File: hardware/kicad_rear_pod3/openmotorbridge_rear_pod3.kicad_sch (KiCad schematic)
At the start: 9 parts, among them J1 POGO_6PIN_MATRIX, J3 MM8030_2G4, J4 MM8030_LORA, J5 MM8030_GNSS, U1 ESP32-C3-WROOM-02U, U2 MAX-M10S, U3 SX1262, U4 DS2401

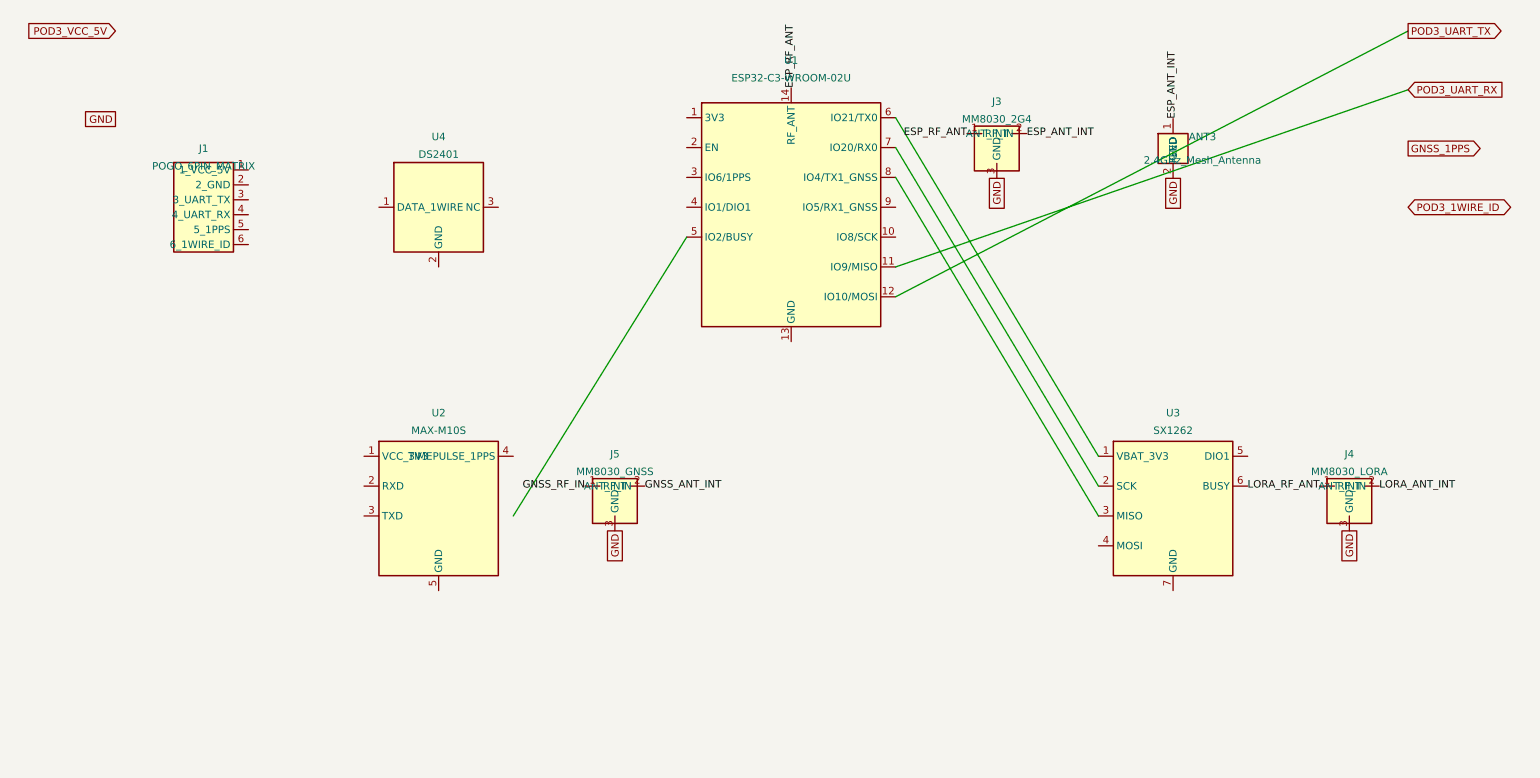
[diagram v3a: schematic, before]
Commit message: feat(pcb): resize OMM transceiver board to 55x48mm and pre-place components
- Resized Edge.Cuts to 55.0 x 48.0 mm (R = 2.5 mm)
- Removed obsolete chip antennas (ANT1, ANT2, ANT3) and mechanical switch (J3)
- Replaced J4 (LoRa) and J5 (GNSS) with U.FL footprints
- Replaced U1 with ESP32-C3-WROOM-02U footprint
- Positioned 4x M2 mounting holes matching sled standoffs: H1/H2 at X=103mm, H3/H4 at X=149mm
- Pre-placed components into clean functional zones (Interface, GNSS, LoRa, ESP32)
- Re-rendered photorealistic top and bottom 3D raytraces
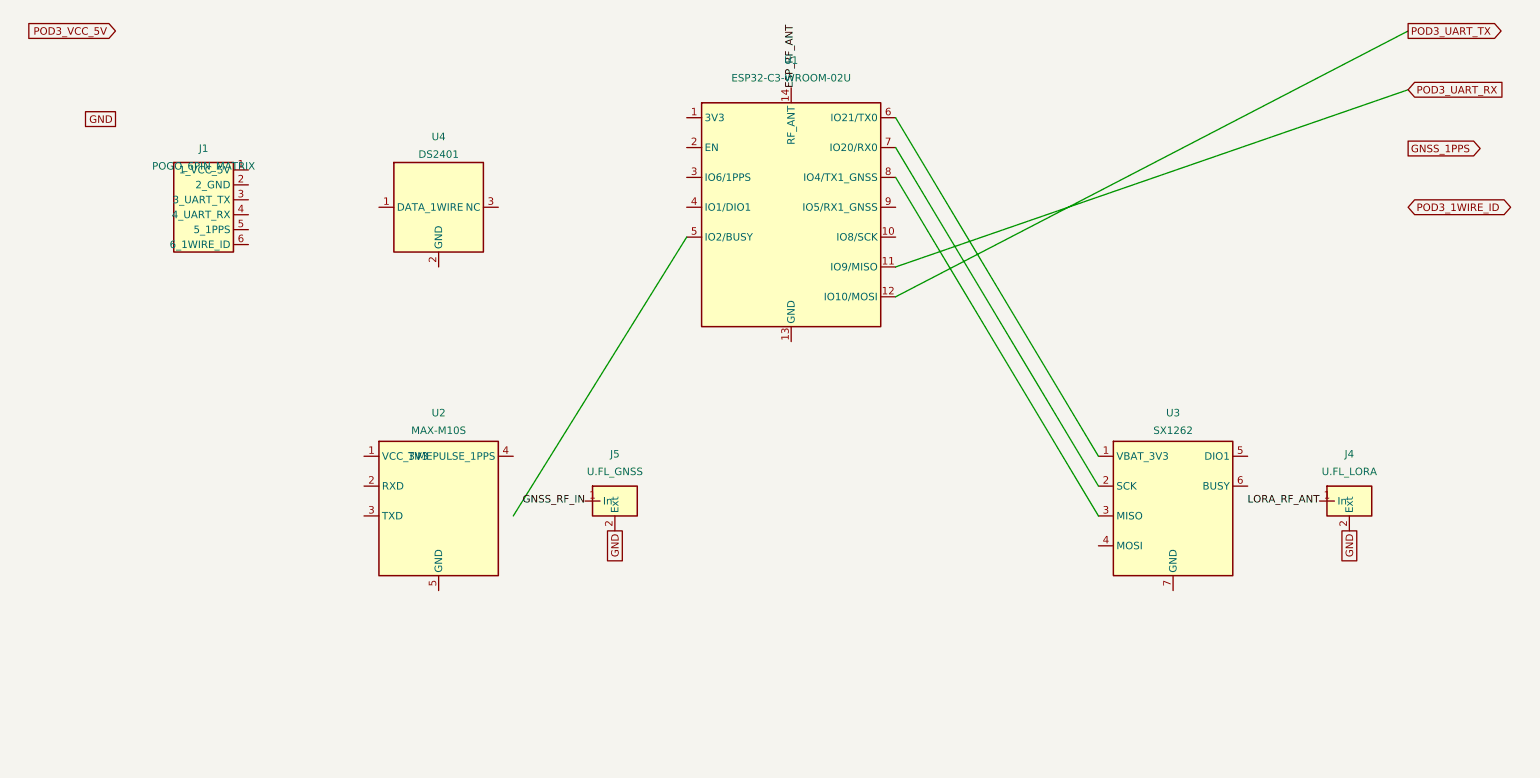
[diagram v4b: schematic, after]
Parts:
- removed ANT3: 2.4GHz_Mesh_Antenna, symbol RF_Antenna:Pulse_W3000
- removed J3: MM8030_2G4, symbol Connector_Coaxial:Murata_MM8030
- J4: value MM8030_LORA -> U.FL_LORA; symbol Connector_Coaxial:Murata_MM8030 -> Connector_Coaxial:U.FL
- J5: value MM8030_GNSS -> U.FL_GNSS; symbol Connector_Coaxial:Murata_MM8030 -> Connector_Coaxial:U.FL
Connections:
- net GNSS_ANT_INT is gone; now on net GND: J5.2 (Ext)
- net LORA_ANT_INT is gone; now on net GND: J4.2 (Ext)
- net GND: no longer J4.3 (GND), J5.3 (GND)
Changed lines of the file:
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@@
 	(wire (pts (xy 162.78 54.76) (xy 197.3 112.38)) (stroke (width 0) (type solid)))
 	(wire (pts (xy 97.7 122.54) (xy 127.22 75.08)) (stroke (width 0) (type solid)))
-	(symbol (lib_id "Connector_Coaxial:Murata_MM8030") (at 180.0 60.0 0) (unit 1)
-		(in_bom yes) (on_board yes) (dnp no)
-		(property "Reference" "J3" (at 180.0 52.0 0) (effects (font (size 1.27 1.27))))
-		(property "Value" "MM8030_2G4" (at 180.0 55.0 0) (effects (font (size 1.27 1.27))))
-		(pin "1")
-		(pin "2")
-		(pin "3")
-	)
-	(label "ESP_RF_ANT" (at 174.92 57.46 180) (effects (font (size 1.27 1.27)) (justify right)))
-	(label "ESP_ANT_INT" (at 185.08 57.46 0) (effects (font (size 1.27 1.27)) (justify left)))
-	(global_label "GND" (shape passive) (at 180.0 65.08 270) (effects (font (size 1.27 1.27))))
-	(symbol (lib_id "Connector_Coaxial:Murata_MM8030") (at 240.0 120.0 0) (unit 1)
+	(symbol (lib_id "Connector_Coaxial:U.FL") (at 240.0 120.0 0) (unit 1)
 		(in_bom yes) (on_board yes) (dnp no)
 		(property "Reference" "J4" (at 240.0 112.0 0) (effects (font (size 1.27 1.27))))
-		(property "Value" "MM8030_LORA" (at 240.0 115.0 0) (effects (font (size 1.27 1.27))))
-		(pin "1")
-		(pin "2")
-		(pin "3")
-	)
-	(label "LORA_RF_ANT" (at 234.92 117.46 180) (effects (font (size 1.27 1.27)) (justify right)))
-	(label "LORA_ANT_INT" (at 245.08 117.46 0) (effects (font (size 1.27 1.27)) (justify left)))
-	(global_label "GND" (shape passive) (at 240.0 125.08 270) (effects (font (size 1.27 1.27))))
-	(symbol (lib_id "Connector_Coaxial:Murata_MM8030") (at 115.0 120.0 0) (unit 1)
-		(in_bom yes) (on_board yes) (dnp no)
-		(property "Reference" "J5" (at 115.0 112.0 0) (effects (font (size 1.27 1.27))))
-		(property "Value" "MM8030_GNSS" (at 115.0 115.0 0) (effects (font (size 1.27 1.27))))
-		(pin "1")
-		(pin "2")
-		(pin "3")
-	)
-	(label "GNSS_RF_IN" (at 109.92 117.46 180) (effects (font (size 1.27 1.27)) (justify right)))
-	(label "GNSS_ANT_INT" (at 120.08 117.46 0) (effects (font (size 1.27 1.27)) (justify left)))
-	(global_label "GND" (shape passive) (at 115.0 125.08 270) (effects (font (size 1.27 1.27))))
-	(symbol (lib_id "RF_Antenna:Pulse_W3000") (at 210.0 60.0 0) (unit 1)
-		(in_bom yes) (on_board yes) (dnp no)
-		(property "Reference" "ANT3" (at 215.0 58.0 0) (effects (font (size 1.27 1.27))))
-		(property "Value" "2.4GHz_Mesh_Antenna" (at 215.0 62.0 0) (effects (font (size 1.27 1.27))))
+		(property "Value" "U.FL_LORA" (at 240.0 115.0 0) (effects (font (size 1.27 1.27))))
 		(pin "1")
 		(pin "2")
 	)
-	(label "ESP_ANT_INT" (at 210.0 54.92 90) (effects (font (size 1.27 1.27)) (justify left)))
-	(global_label "GND" (shape passive) (at 210.0 65.08 270) (effects (font (size 1.27 1.27))))
+	(label "LORA_RF_ANT" (at 234.92 120.0 180) (effects (font (size 1.27 1.27)) (justify right)))
+	(global_label "GND" (shape passive) (at 240.0 125.08 270) (effects (font (size 1.27 1.27))))
+	(symbol (lib_id "Connector_Coaxial:U.FL") (at 115.0 120.0 0) (unit 1)
+		(in_bom yes) (on_board yes) (dnp no)
+		(property "Reference" "J5" (at 115.0 112.0 0) (effects (font (size 1.27 1.27))))
+		(property "Value" "U.FL_GNSS" (at 115.0 115.0 0) (effects (font (size 1.27 1.27))))
+		(pin "1")
+		(pin "2")
+	)
+	(label "GNSS_RF_IN" (at 109.92 120.0 180) (effects (font (size 1.27 1.27)) (justify right)))
+	(global_label "GND" (shape passive) (at 115.0 125.08 270) (effects (font (size 1.27 1.27))))
 )

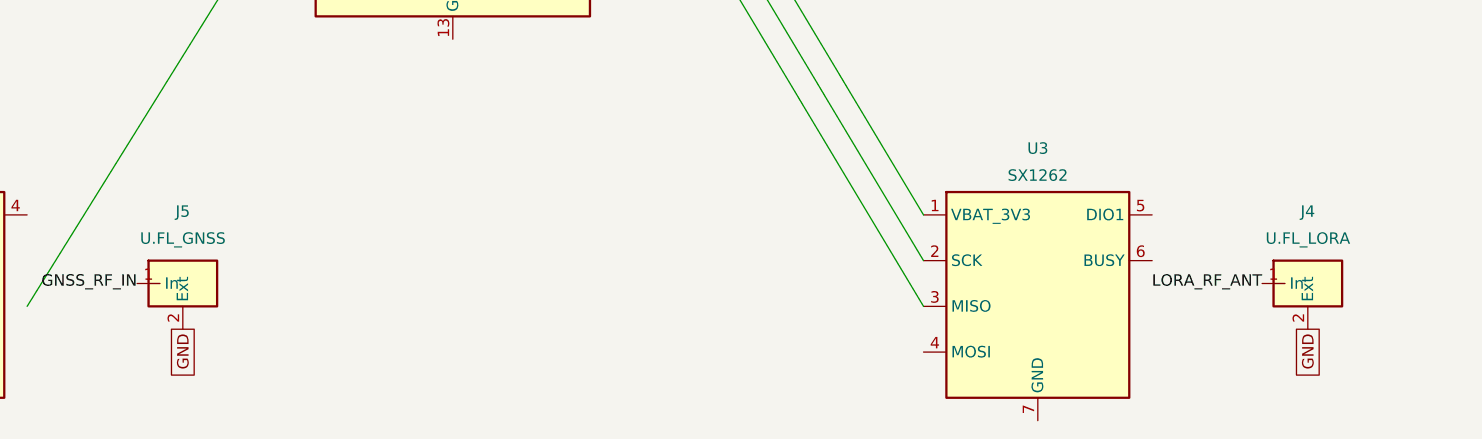
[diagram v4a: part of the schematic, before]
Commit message: fix(pcb): connect J4 and J5 U.FL shield pads to GND net
- Fixed pin 2 orientation in Connector_Coaxial:U.FL schematic symbol
- Assigned Net GND to both outer shield pads of J4 (LoRa) and J5 (GNSS)
- Regenerated 3D raytrace render
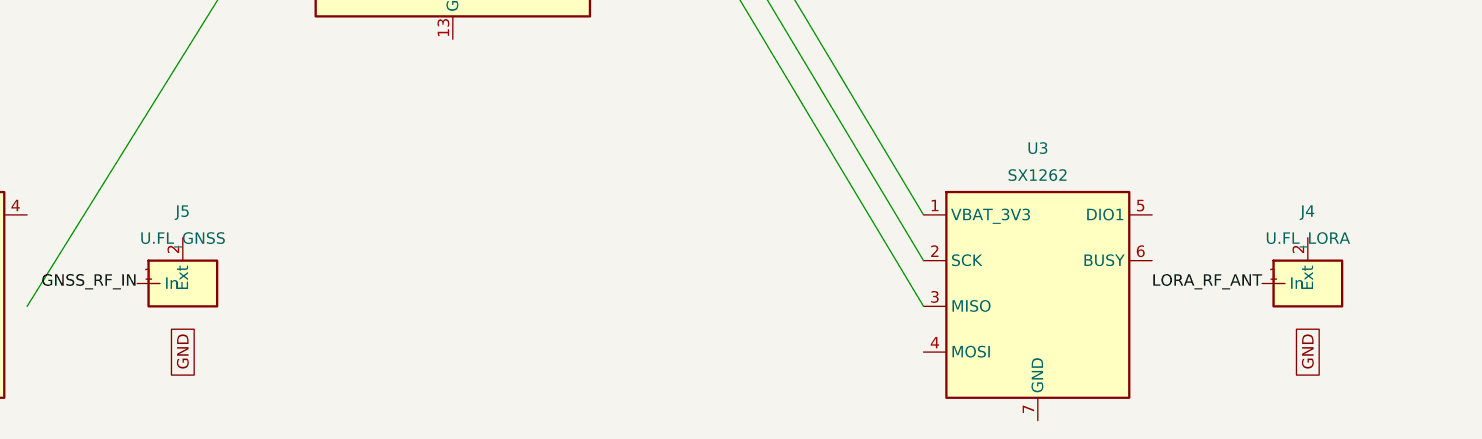
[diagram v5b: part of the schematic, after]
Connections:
- net GND: no longer J4.2 (Ext), J5.2 (Ext)
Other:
- moved on the sheet: J4, J5

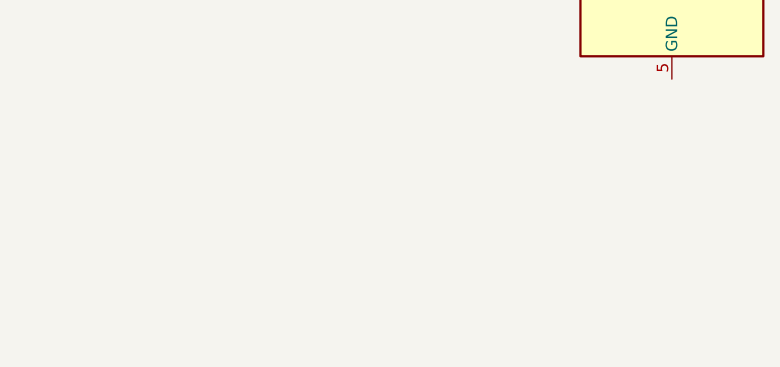
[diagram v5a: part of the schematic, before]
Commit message: feat(hardware,mechatronics): integrate Radar 2.0 winged housing, Garmin bayonet mount, PCBA 08 routed board with ESP32-C5 V2X & manufacturing packages
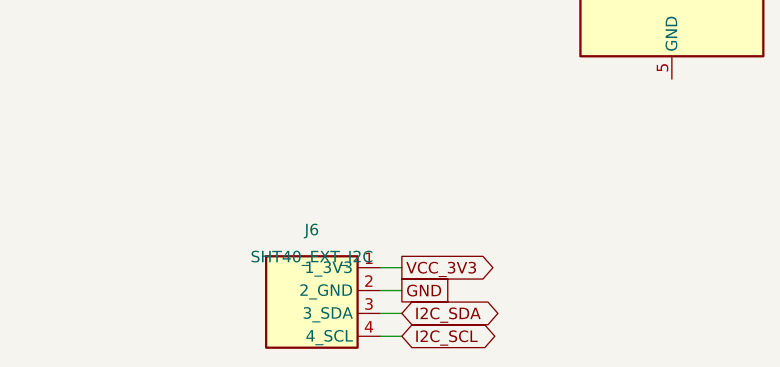
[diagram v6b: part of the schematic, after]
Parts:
- added J6: SHT40_EXT_I2C, symbol Connector:Conn_01x04
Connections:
- net GND: now also J6.2 (2_GND)
- new net I2C_SCL: J6.4 (4_SCL)
- new net I2C_SDA: J6.3 (3_SDA)
- new net VCC_3V3: J6.1 (1_3V3)
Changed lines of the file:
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@@
 	(label "GNSS_RF_IN" (at 109.92 120.0 180) (effects (font (size 1.27 1.27)) (justify right)))
 	(global_label "GND" (shape passive) (at 115.0 125.08 270) (effects (font (size 1.27 1.27))))
+	(symbol (lib_id "Connector:Conn_01x04") (at 45.0 160.0 0) (unit 1)
+		(in_bom yes) (on_board yes) (dnp no)
+		(property "Reference" "J6" (at 45.0 152.0 0) (effects (font (size 1.27 1.27))))
+		(property "Value" "SHT40_EXT_I2C" (at 45.0 155.0 0) (effects (font (size 1.27 1.27))))
+		(pin "1")
+		(pin "2")
+		(pin "3")
+		(pin "4")
+	)
+	(global_label "VCC_3V3" (shape output) (at 55.0 156.19 0) (effects (font (size 1.27 1.27))))
+	(global_label "GND" (shape passive) (at 55.0 158.73 0) (effects (font (size 1.27 1.27))))
+	(global_label "I2C_SDA" (shape bidirectional) (at 55.0 161.27 0) (effects (font (size 1.27 1.27))))
+	(global_label "I2C_SCL" (shape bidirectional) (at 55.0 163.81 0) (effects (font (size 1.27 1.27))))
+	(wire (pts (xy 52.62 156.19) (xy 55.0 156.19)) (stroke (width 0) (type solid)))
+	(wire (pts (xy 52.62 158.73) (xy 55.0 158.73)) (stroke (width 0) (type solid)))
+	(wire (pts (xy 52.62 161.27) (xy 55.0 161.27)) (stroke (width 0) (type solid)))
+	(wire (pts (xy 52.62 163.81) (xy 55.0 163.81)) (stroke (width 0) (type solid)))
 )

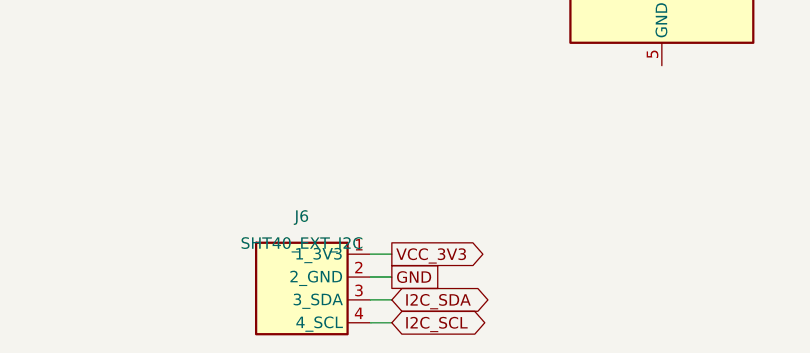
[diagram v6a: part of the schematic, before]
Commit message: hardware: integrate J6 1-Wire DS18B20 temperature port into Rear Pod 3 PCBA and harmonize docs
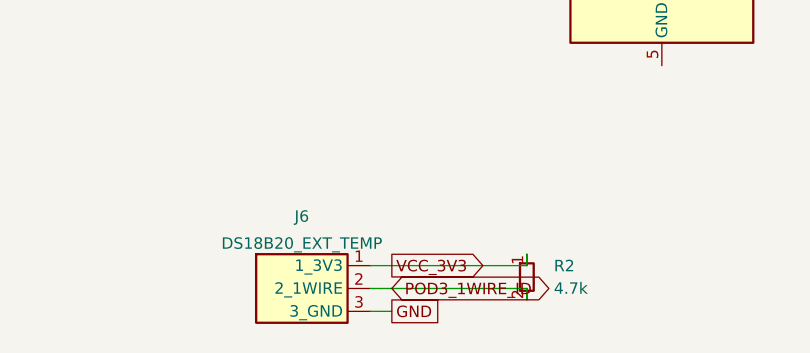
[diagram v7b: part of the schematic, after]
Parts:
- added R2: 4.7k, Resistor_SMD:R_0603_1608Metric, symbol Device:R_Small
- J6: value SHT40_EXT_I2C -> DS18B20_EXT_TEMP; footprint (none) -> Connector_JST:JST_SH_SM03B-SRSS-TB_1x03-1MP_P1.00mm_Horizontal; symbol Connector:Conn_01x04 -> Connector:Conn_01x03; LCSC (none) -> C136656
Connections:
- net I2C_SDA is gone; now on net GND: J6.3 (3_GND)
- net GND: no longer J6.2 (2_GND)
- net POD3_1WIRE_ID: now also J6.2 (2_1WIRE), R2.2
- net VCC_3V3: now also R2.1
- removed net I2C_SCL: J6.4 (4_SCL)
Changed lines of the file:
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@@
 	(label "GNSS_RF_IN" (at 109.92 120.0 180) (effects (font (size 1.27 1.27)) (justify right)))
 	(global_label "GND" (shape passive) (at 115.0 125.08 270) (effects (font (size 1.27 1.27))))
-	(symbol (lib_id "Connector:Conn_01x04") (at 45.0 160.0 0) (unit 1)
+	(symbol (lib_id "Connector:Conn_01x03") (at 45.0 160.0 0) (unit 1)
 		(in_bom yes) (on_board yes) (dnp no)
 		(property "Reference" "J6" (at 45.0 152.0 0) (effects (font (size 1.27 1.27))))
-		(property "Value" "SHT40_EXT_I2C" (at 45.0 155.0 0) (effects (font (size 1.27 1.27))))
+		(property "Value" "DS18B20_EXT_TEMP" (at 45.0 155.0 0) (effects (font (size 1.27 1.27))))
+		(property "Footprint" "Connector_JST:JST_SH_SM03B-SRSS-TB_1x03-1MP_P1.00mm_Horizontal" (at 0 0 0) (effects (font (size 1.27 1.27)) hide))
+		(property "LCSC" "C136656" (at 0 0 0) (effects (font (size 1.27 1.27)) hide))
 		(pin "1")
 		(pin "2")
 		(pin "3")
-		(pin "4")
 	)
-	(global_label "VCC_3V3" (shape output) (at 55.0 156.19 0) (effects (font (size 1.27 1.27))))
-	(global_label "GND" (shape passive) (at 55.0 158.73 0) (effects (font (size 1.27 1.27))))
-	(global_label "I2C_SDA" (shape bidirectional) (at 55.0 161.27 0) (effects (font (size 1.27 1.27))))
-	(global_label "I2C_SCL" (shape bidirectional) (at 55.0 163.81 0) (effects (font (size 1.27 1.27))))
-	(wire (pts (xy 52.62 156.19) (xy 55.0 156.19)) (stroke (width 0) (type solid)))
-	(wire (pts (xy 52.62 158.73) (xy 55.0 158.73)) (stroke (width 0) (type solid)))
-	(wire (pts (xy 52.62 161.27) (xy 55.0 161.27)) (stroke (width 0) (type solid)))
-	(wire (pts (xy 52.62 163.81) (xy 55.0 163.81)) (stroke (width 0) (type solid)))
+	(global_label "VCC_3V3" (shape output) (at 55.0 157.46 0) (effects (font (size 1.27 1.27))))
+	(global_label "POD3_1WIRE_ID" (shape bidirectional) (at 55.0 160.0 0) (effects (font (size 1.27 1.27))))
+	(global_label "GND" (shape passive) (at 55.0 162.54 0) (effects (font (size 1.27 1.27))))
+	(wire (pts (xy 52.62 157.46) (xy 55.0 157.46)) (stroke (width 0) (type solid)))
+	(wire (pts (xy 52.62 160.0) (xy 55.0 160.0)) (stroke (width 0) (type solid)))
+	(wire (pts (xy 52.62 162.54) (xy 55.0 162.54)) (stroke (width 0) (type solid)))
+	(symbol (lib_id "Device:R_Small") (at 70.0 158.73 0) (unit 1)
+		(in_bom yes) (on_board yes) (dnp no)
+		(property "Reference" "R2" (at 73.0 157.5 0) (effects (font (size 1.27 1.27)) (justify left)))
+		(property "Value" "4.7k" (at 73.0 160.0 0) (effects (font (size 1.27 1.27)) (justify left)))
+		(property "Footprint" "Resistor_SMD:R_0603_1608Metric" (at 0 0 0) (effects (font (size 1.27 1.27)) hide))
+		(property "LCSC" "C23164" (at 0 0 0) (effects (font (size 1.27 1.27)) hide))
+		(pin "1")
+		(pin "2")
+	)
+	(wire (pts (xy 70.0 156.19) (xy 70.0 157.46)) (stroke (width 0) (type solid)))
+	(wire (pts (xy 70.0 157.46) (xy 55.0 157.46)) (stroke (width 0) (type solid)))
+	(wire (pts (xy 70.0 161.27) (xy 70.0 160.0)) (stroke (width 0) (type solid)))
+	(wire (pts (xy 70.0 160.0) (xy 55.0 160.0)) (stroke (width 0) (type solid)))
 )
